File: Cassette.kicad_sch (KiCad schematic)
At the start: 46 parts, among them J3 Front View, K1 Relay_SPST-NO

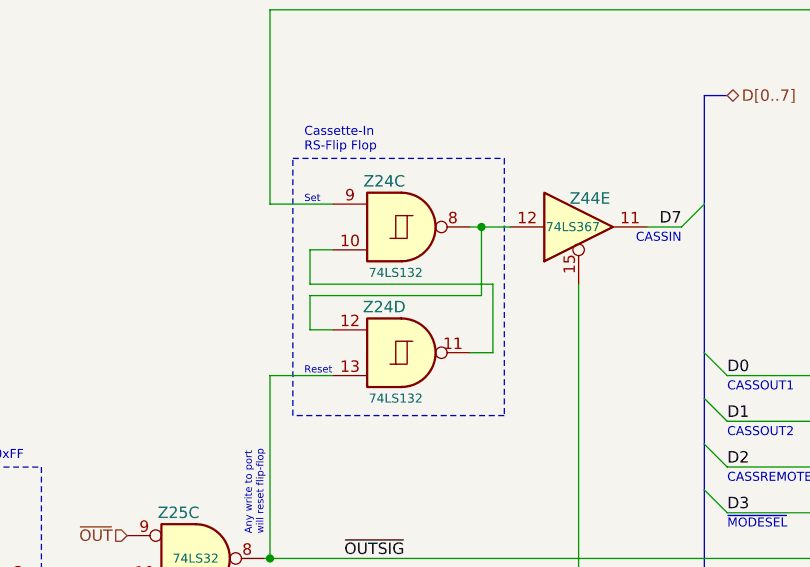
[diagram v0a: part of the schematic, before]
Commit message: Fix CASSIN Flip-Flop description
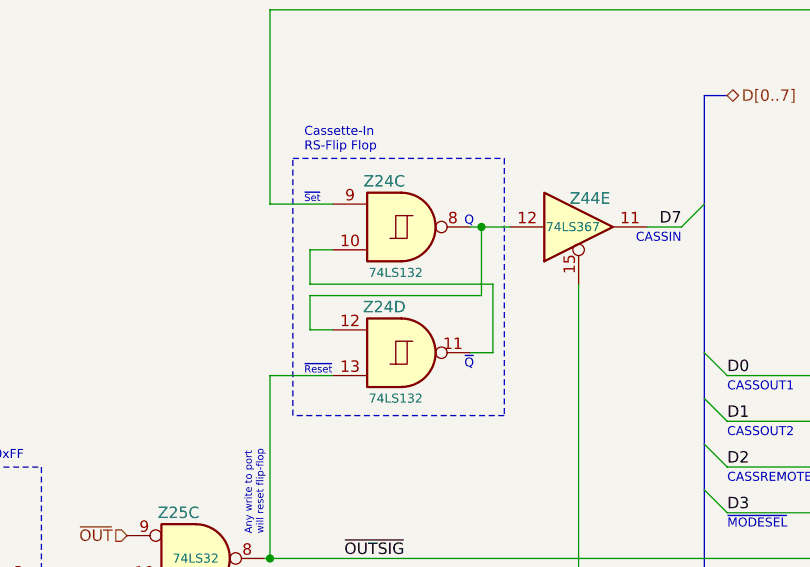
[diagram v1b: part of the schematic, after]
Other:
- note added: "Q"
- note added: "~{Q}"
- note added: "~{Reset}"
- note added: "~{Set}"
- note removed: "Reset"
- note removed: "Set"
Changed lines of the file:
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@@
+    (effects (font (size 1 1)) (justify left bottom))
+  )
+  (text "~{Q}" (at 111.76 115.57 0)
+    (effects (font (size 1 1)) (justify left bottom))
+  )
+  (text "Q" (at 111.76 99.695 0)
     (effects (font (size 1 1)) (justify left bottom))
   )
@@
     (effects (font (size 1 1)) (justify left bottom))
   )
-  (text "Reset" (at 93.98 116.205 0)
+  (text "~{Reset}" (at 93.98 116.205 0)
     (effects (font (size 0.8 0.8)) (justify left bottom))
   )
-  (text "Set" (at 93.98 97.155 0)
+  (text "~{Set}" (at 93.98 97.155 0)
     (effects (font (size 0.8 0.8)) (justify left bottom))
   )
